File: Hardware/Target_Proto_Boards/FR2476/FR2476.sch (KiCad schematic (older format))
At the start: 44 parts, among them J1 USB_B_Micro, J10 PORT6, J11 PORT3, J12 JTAG/SBW, J13 VSEL, J14 VCC, J15 GND, J16 +5V, J17 GND, J4 LED_P4.1, J5 DEBUG, J6 PORT4, J7 PORT1, J8 PORT5, J9 PORT2, SW1 TL-2203, SW2 RESET, U1 MSP430FR2476TPTR, U2 HT7533-1, Y1 32768 12pF

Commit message: Updated Hardware Schematics and Boards
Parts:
- removed RN1, RN2: 4x470, lib:R_Array_Convex_4x0603_handsoldered, symbol Device:R_Pack04
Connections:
- net P1.5 is gone; now on net P1.5_TDO: J7.6 (Pin_6), U1.5 (P1-5_UCA0RXD_UCA0SOMI_TA1-1_TMS_A5)
- net P1.6 is gone; now on net P1.6_TDI: J7.7 (Pin_7), U1.6 (P1-6_UCA0CLK_TA1CLK_TDI_TCLK_A6)
- net P5.1 is gone; now on net JRXD: J8.2 (Pin_2), U1.44 (P5-1_UCA0RXD_UCA0SOMI_TB0-3)
- net P5.2 is gone; now on net JTXD: J8.3 (Pin_3), U1.45 (P5-2_UCA0TXD_UCA0SIMO_TB0-4)
- net RRST is gone; now on net JRST: J5.11 (Pin_11), J5.5 (Pin_5)
- net RTCK is gone; now on net JTCK: J5.3 (Pin_3), J5.9 (Pin_9)
- net RTDO is gone; now on net JTDO: J5.1 (Pin_1), J5.7 (Pin_7)
- net RTEST is gone; now on net JTEST: J5.13 (Pin_13)
- net JTDI renamed P1.6_TDI
- net JTMS renamed P1.5_TDO
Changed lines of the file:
@@
 	9850 5850 10100 5850
 Wire Wire Line
-	9350 5550 9150 5550
+	9350 5550 9050 5550
 Text Label 10100 5550 2    50   ~ 0
 JTEST
@@
 Wire Wire Line
 	9100 5850 9100 5900
-Text Label 9150 5550 0    50   ~ 0
+Text Label 9050 5550 0    50   ~ 0
 JTCK
 $Comp
@@
 	1150 2550 900  2550
 Wire Wire Line
-	1150 2450 900  2450
-Wire Wire Line
-	1150 2350 900  2350
+	1150 2450 750  2450
+Wire Wire Line
+	1150 2350 750  2350
 Wire Wire Line
 	1150 2250 900  2250
@@
 Text Label 900  2250 0    50   ~ 0
 P1.4
-Text Label 900  2350 0    50   ~ 0
-P1.5
-Text Label 900  2450 0    50   ~ 0
-P1.6
+Text Label 750  2350 0    50   ~ 0
+P1.5_TDO
+Text Label 750  2450 0    50   ~ 0
+P1.6_TDI
 Text Label 900  2550 0    50   ~ 0
 P1.7
@@
 	7300 1450 7050 1450
 Wire Wire Line
-	7300 1550 7050 1550
-Wire Wire Line
-	7300 1650 7050 1650
+	7300 1550 6950 1550
+Wire Wire Line
+	7300 1650 6950 1650
 Wire Wire Line
 	7300 1750 7050 1750
@@
 Text Label 7050 1450 0    50   ~ 0
 P1.4
-Text Label 7050 1550 0    50   ~ 0
-P1.5
-Text Label 7050 1650 0    50   ~ 0
-P1.6
+Text Label 6950 1550 0    50   ~ 0
+P1.5_TDO
+Text Label 6950 1650 0    50   ~ 0
+P1.6_TDI
 Text Label 7050 1750 0    50   ~ 0
 P1.7
@@
 P5.0
 Text Label 7950 2300 0    50   ~ 0
-P5.1
+JRXD
 Text Label 7950 2400 0    50   ~ 0
-P5.2
+JTXD
 Text Label 7950 2500 0    50   ~ 0
 P5.3
@@
 P5.0
 Text Label 900  3750 0    50   ~ 0
-P5.1
+JRXD
 Text Label 900  3850 0    50   ~ 0
-P5.2
+JTXD
 Text Label 900  3950 0    50   ~ 0
 P5.3
@@
 Wire Wire Line
 	4150 5400 4250 5400
-Text Label 8000 6050 0    50   ~ 0
-P5.2
-Text Label 8000 6150 0    50   ~ 0
-P5.1
 Text Label 9850 5250 0    50   ~ 0
 VCC_TOOL
@@
 	5600 4350 5550 4350
 Wire Wire Line
-	9150 5250 9350 5250
+	9050 5250 9350 5250
 Wire Wire Line
 	9150 5750 9350 5750
@@
 Text Label 9150 5750 0    50   ~ 0
 JRST
-Text Label 8900 5550 2    50   ~ 0
-JTDO
 NoConn ~ 1150 1650
 Wire Wire Line
@@
 Text Label 5850 3850 2    50   ~ 0
 TEST
-$Comp
-L Device:R_Pack04 RN1
-U 1 1 6192A320
-P 8450 5450
-F 0 "RN1" V 8150 5350 50  0000 L CNN
-F 1 "4x470" V 8650 5350 50  0000 L CNN
-F 2 "lib:R_Array_Convex_4x0603_handsoldered" V 8725 5450 50  0001 C CNN
-F 3 "~" H 8450 5450 50  0001 C CNN
-F 4 "C25510" H 8450 5450 50  0001 C CNN "LCSC"
-F 5 "1206 Resistor Networks & Arrays ROHS" H 8450 5450 50  0001 C CNN "Descr"
-	1    8450 5450
-	0    1    1    0
-$EndComp
-Wire Wire Line
-	9350 5350 9150 5350
-Wire Wire Line
-	9350 5450 9150 5450
-Text Label 9150 5350 0    50   ~ 0
-JTDI
-Text Label 9150 5450 0    50   ~ 0
-JTMS
-Wire Wire Line
-	8250 5250 8000 5250
-Wire Wire Line
-	8250 5350 8000 5350
-Wire Wire Line
-	8250 5450 8000 5450
-Wire Wire Line
-	8250 5550 8000 5550
+Wire Wire Line
+	9350 5350 9050 5350
+Wire Wire Line
+	9350 5450 9050 5450
+Text Label 9050 5350 0    50   ~ 0
+P1.6_TDI
+Text Label 9050 5450 0    50   ~ 0
+P1.5_TDO
 $Comp
 L Connector_Generic:Conn_02x07_Odd_Even J5
@@
 	1    0    0    -1
 $EndComp
-$Comp
-L Device:R_Pack04 RN2
-U 1 1 612D1637
-P 8450 6050
-F 0 "RN2" V 8150 5950 50  0000 L CNN
-F 1 "4x470" V 8650 5950 50  0000 L CNN
-F 2 "lib:R_Array_Convex_4x0603_handsoldered" V 8725 6050 50  0001 C CNN
-F 3 "~" H 8450 6050 50  0001 C CNN
-F 4 "C25510" H 8450 6050 50  0001 C CNN "LCSC"
-F 5 "1206 Resistor Networks & Arrays ROHS" H 8450 6050 50  0001 C CNN "Descr"
-	1    8450 6050
-	0    1    1    0
-$EndComp
-Wire Wire Line
-	8900 5850 8650 5850
-Text Label 8900 5850 2    50   ~ 0
-JTEST
-Wire Wire Line
-	8650 5950 8900 5950
-Wire Wire Line
-	8250 5950 8000 5950
-Wire Wire Line
-	8250 5850 8000 5850
-Wire Wire Line
-	8250 6050 8000 6050
-Wire Wire Line
-	8250 6150 8000 6150
 Text Label 10100 5750 2    50   ~ 0
 JTXD
@@
 JRXD
 Wire Wire Line
-	8650 6050 8900 6050
-Wire Wire Line
-	8650 6150 8900 6150
-Text Label 8900 6050 2    50   ~ 0
-JTXD
-Text Label 8900 6150 2    50   ~ 0
-JRXD
-Wire Wire Line
 	6150 5300 6400 5300
 Wire Wire Line
@@
 Text Label 7400 5600 2    50   ~ 0
 RESET
-Text Label 8000 5550 0    50   ~ 0
-RTDO
 Text Label 6150 5600 0    50   ~ 0
-RTDO
-Text Label 8000 5950 0    50   ~ 0
-RRST
+JTDO
 Text Label 6150 5500 0    50   ~ 0
-RRST
-Text Label 8000 5350 0    50   ~ 0
-P1.5
-Text Label 8000 5250 0    50   ~ 0
-RTCK
+JRST
 Wire Wire Line
 	6150 5500 6400 5500
-Text Label 8000 5850 0    50   ~ 0
-RTEST
 Wire Wire Line
 	6150 5600 6400 5600
@@
 	6150 5700 6400 5700
 Text Label 6150 5300 0    50   ~ 0
-RTDO
+JTDO
 Text Label 7400 5100 2    50   ~ 0
 P1.7
-Text Label 8000 5450 0    50   ~ 0
-P1.6
 Wire Wire Line
 	6150 5800 6400 5800
@@
 RESET
 Text Label 6150 5400 0    50   ~ 0
-RTCK
+JTCK
 Text Label 7400 5200 2    50   ~ 0
 P1.4
@@
 	6150 5900 6400 5900
 Text Label 6150 5800 0    50   ~ 0
-RRST
+JRST
 Text Label 7400 6000 2    50   ~ 0
 RESET
 Text Label 6150 5900 0    50   ~ 0
-RTEST
+JTEST
 Text Label 7400 6100 2    50   ~ 0
 TEST
@@
 TEST
 Text Label 6150 5700 0    50   ~ 0
-RTCK
+JTCK
 Text Notes 7450 5900 2    50   ~ 0
 SBW_OX
@@
 Wire Wire Line
 	7000 6000 7400 6000
-Wire Wire Line
-	8650 5250 8900 5250
-Wire Wire Line
-	8650 5350 8900 5350
-Wire Wire Line
-	8650 5450 8900 5450
-Wire Wire Line
-	8650 5550 8900 5550
-Text Label 9150 5250 0    50   ~ 0
+Text Label 9050 5250 0    50   ~ 0
 JTDO
-Text Label 8900 5450 2    50   ~ 0
-JTDI
-Text Label 8900 5350 2    50   ~ 0
-JTMS
-Text Label 8900 5250 2    50   ~ 0
-JTCK
-Text Label 8900 5950 2    50   ~ 0
-JRST
 Text Label 1850 5400 2    50   ~ 0
 AVCC

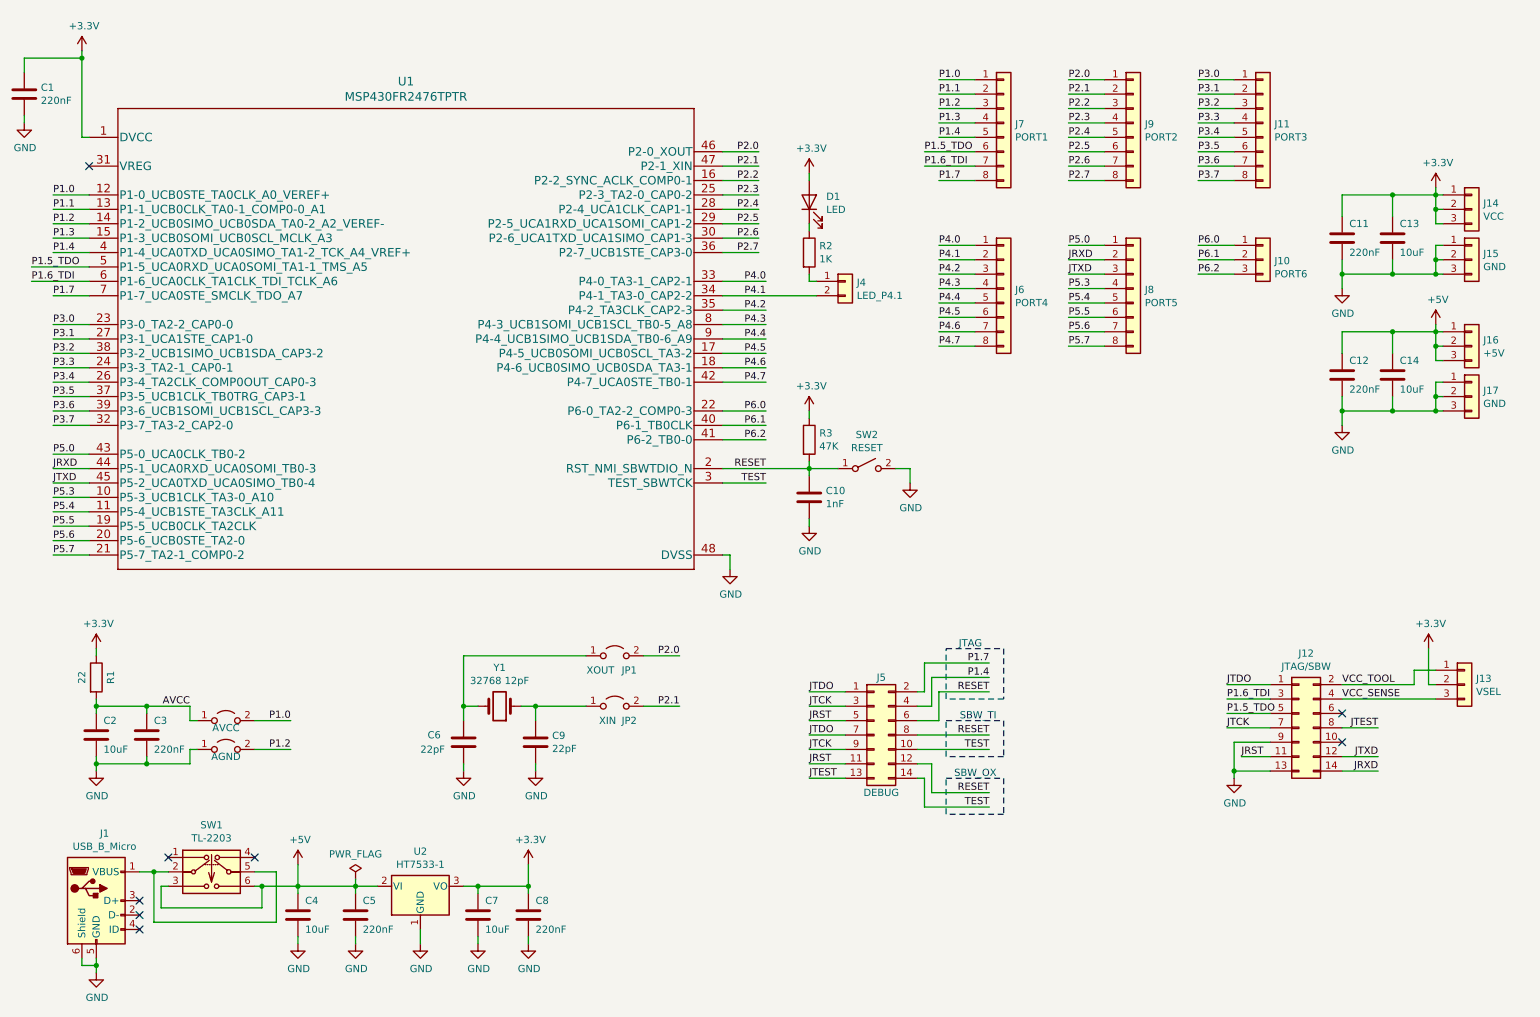
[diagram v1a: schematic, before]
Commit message: Documentation for the MSP430FR2476 Proto board
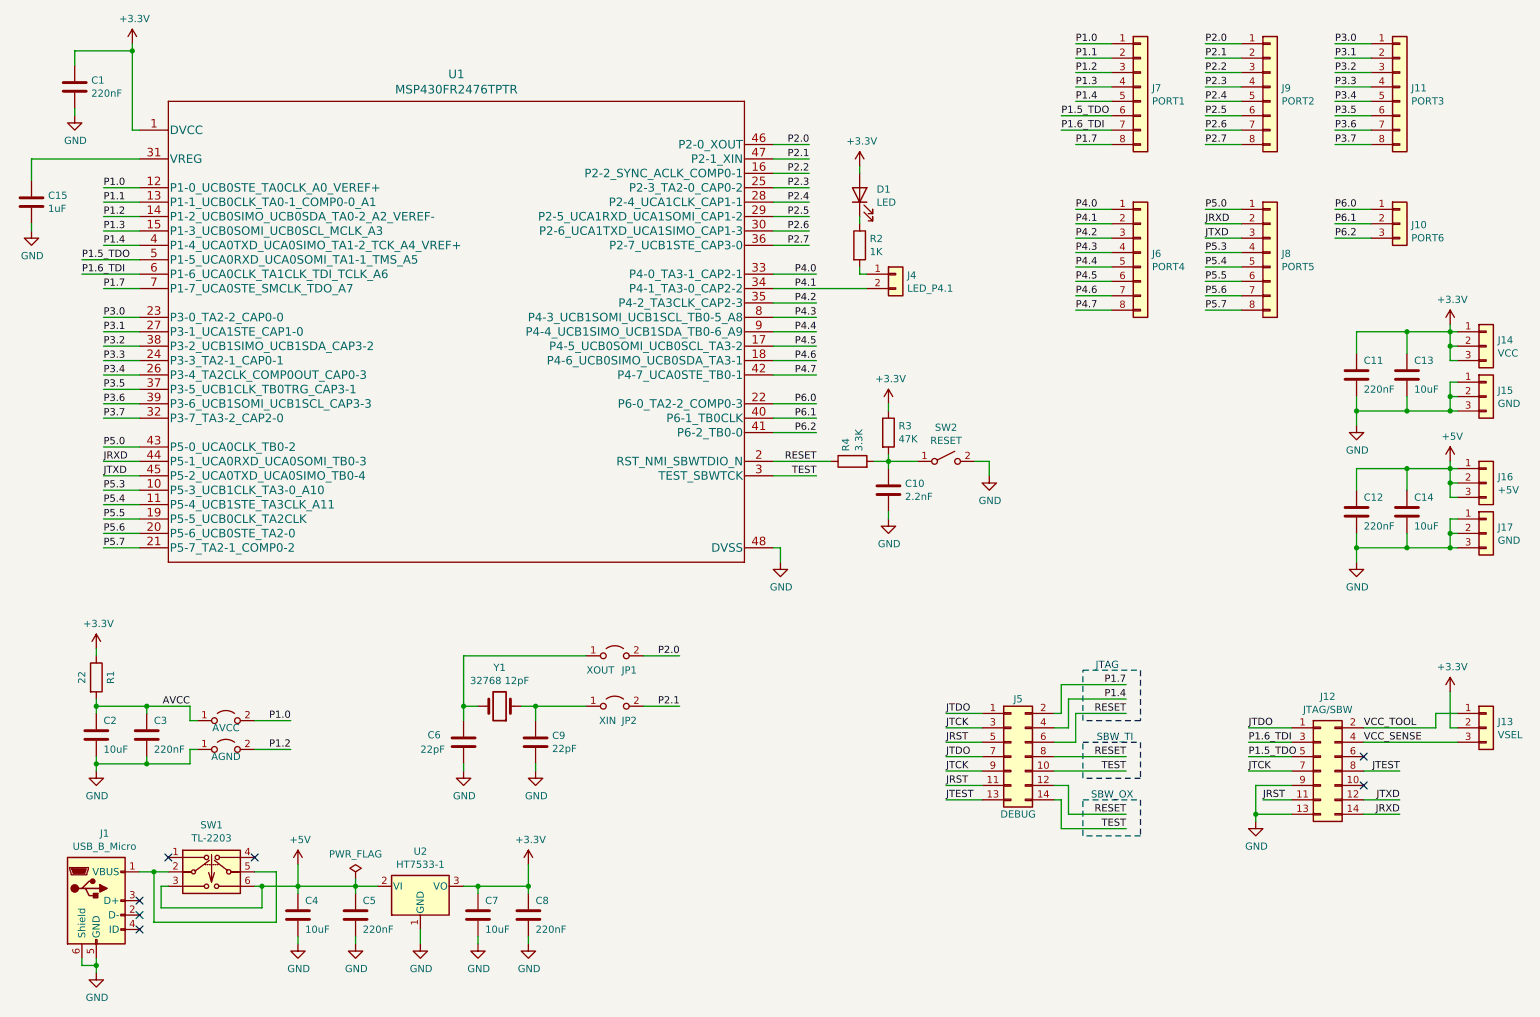
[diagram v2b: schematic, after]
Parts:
- added C15: 1uF, Capacitor_SMD:C_0603_1608Metric_Pad1.08x0.95mm_HandSolder, symbol Device:C
- added R4: 3.3K, Resistor_SMD:R_0603_1608Metric_Pad0.98x0.95mm_HandSolder, symbol Device:R
- C10: value 1nF -> 2.2nF; Descr 0603 Multilayer Ceramic Capacitors MLCC - SMD/SMT ROHS -> X7R 2.2nF ±10% 50V 0603 Multilayer Ceramic Capacitors MLCC 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; LCSC C1588 -> C1604
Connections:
- net GND: now also C15.2
- net RESET: now also R4.1; no longer C10.1, R3.2, SW2.1 (A)
- net at U1.31 (VREG): now also C15.1
- new net: C10.1, R3.2, R4.2, SW2.1 (A)
- no-connect marks 8 -> 7
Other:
- moved on the sheet: C1, C10, C11, C12, C13, C14, D1, J10, J11, J12, J13, J14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
